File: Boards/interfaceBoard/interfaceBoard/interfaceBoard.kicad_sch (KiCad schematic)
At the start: 0 parts

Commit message: interface board work
started interface board with child sheets. Working on MOSI circuit
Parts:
- added D1, D2: LED, symbol Device:LED
- added J1: Interface With Arduino, symbol Connector_Generic:Conn_02x04_Odd_Even
- added R1, R2: R, symbol Device:R
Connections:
- new net: D1.2 (A), R1.2
- new net: D2.2 (A), R2.2
- new net CLK: J1.2 (Pin_2)
- new net GND: D2.1 (K), J1.1 (Pin_1)
- new net LATCH: J1.5 (Pin_5)
- new net LOAD: J1.6 (Pin_6)
- new net MISO: J1.4 (Pin_4)
- new net MOSI: J1.3 (Pin_3)
- new net STATUS: D1.1 (K), J1.7 (Pin_7), R2.1
- new net VCC: J1.8 (Pin_8), R1.1
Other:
- added sheet output (output.kicad_sch)

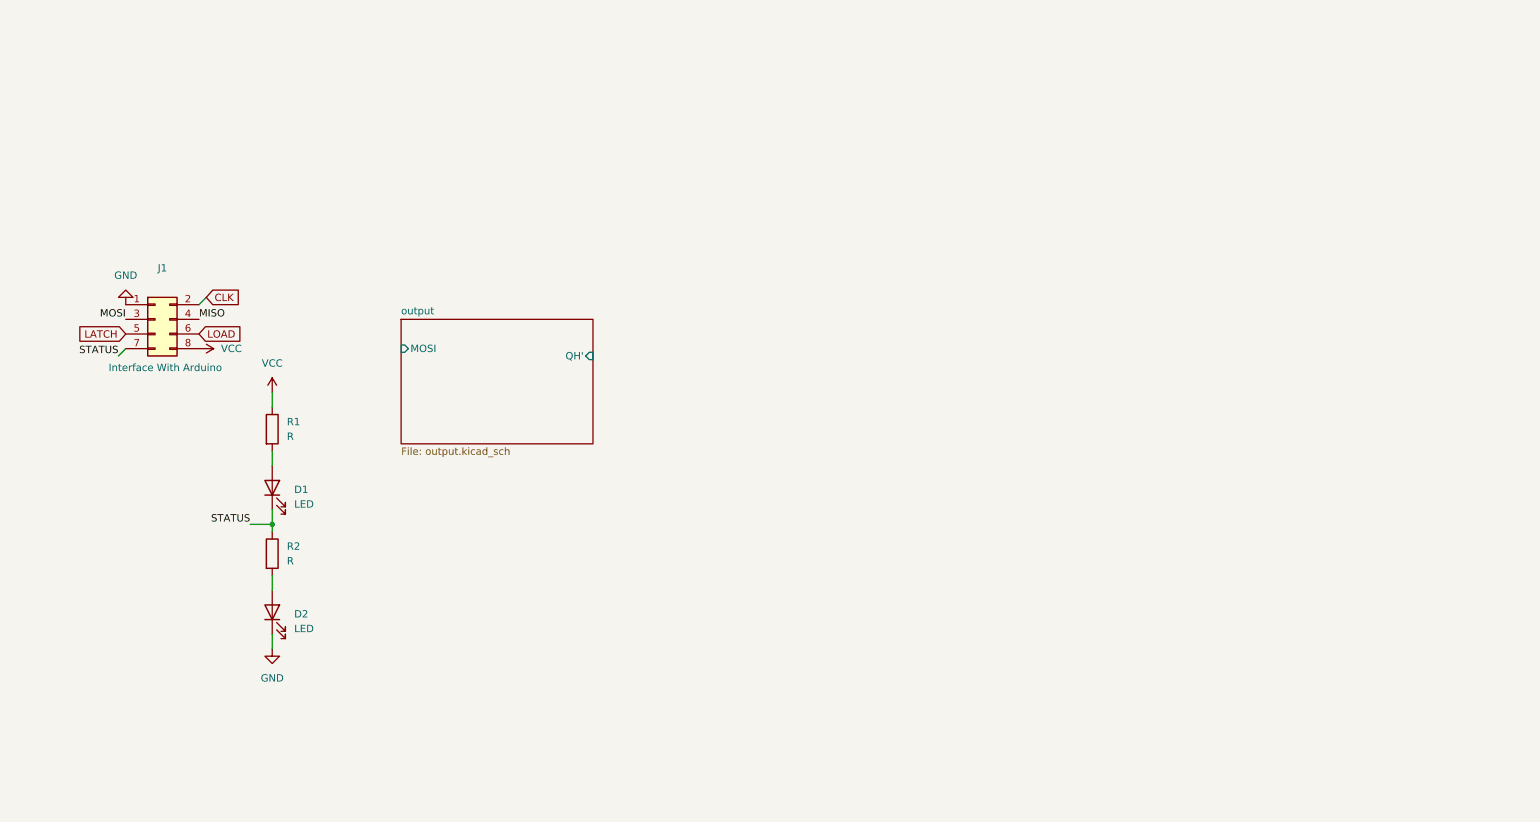
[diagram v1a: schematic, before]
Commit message: interface board work
finished the MOSI child sheet
finished the MISO child sheet
started work on pcb layout (only 1 MOSI and MISO)
started work on pcb layout
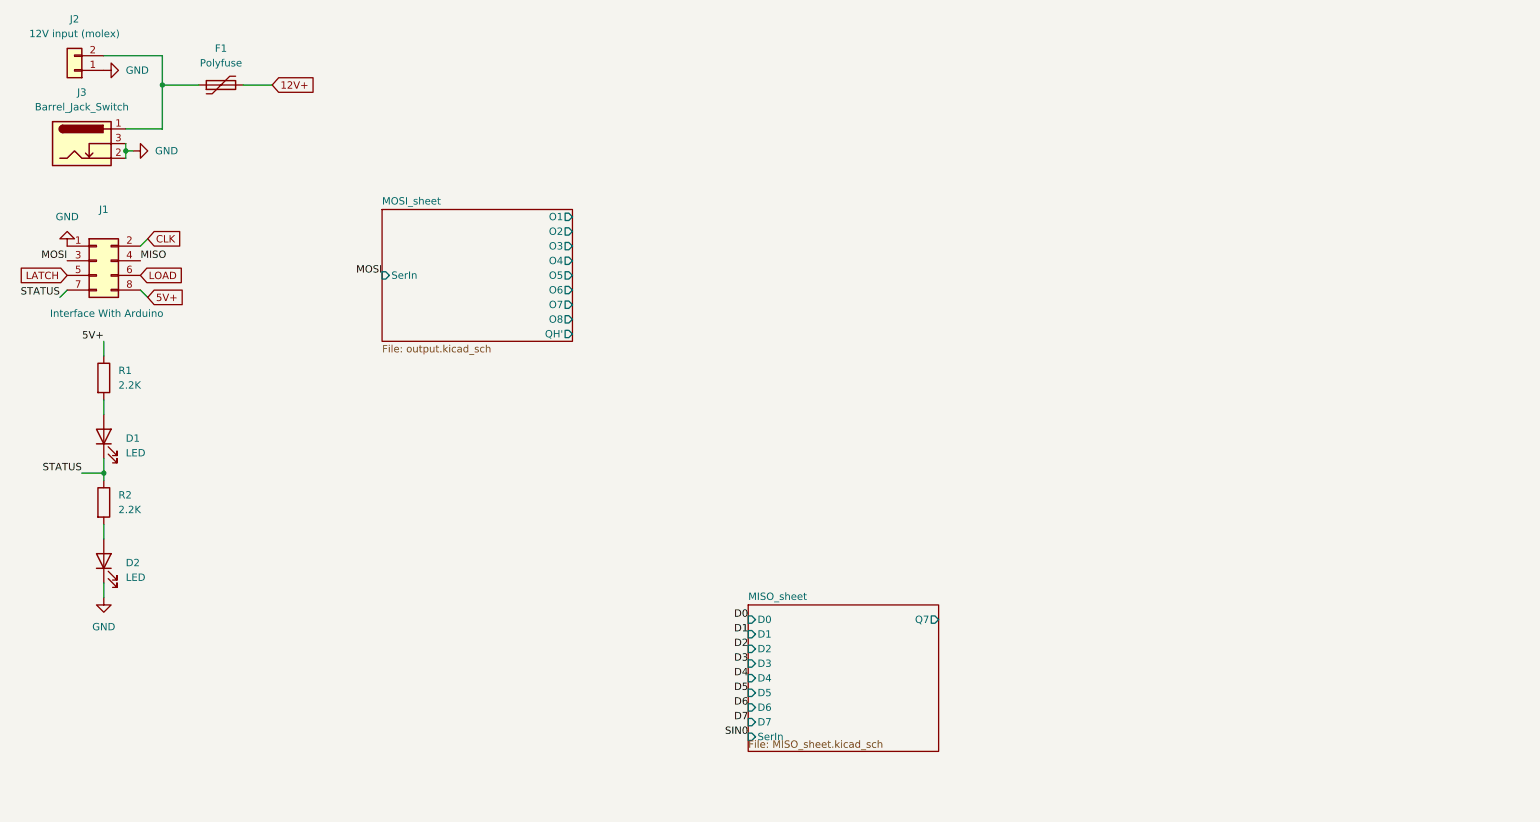
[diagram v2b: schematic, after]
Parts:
- added F1: Polyfuse, Fuse:Fuse_Bourns_MF-RHT100, symbol Device:Polyfuse
- added J2: 12V input (molex), Connector_Molex:Molex_Mini-Fit_Jr_5566-02A_2x01_P4.20mm_Vertical, symbol Connector_Generic:Conn_01x02
- added J3: Barrel_Jack_Switch, Connector_BarrelJack:BarrelJack_Horizontal, symbol Connector:Barrel_Jack_Switch
- D1, D2: footprint (none) -> LED_THT:LED_D3.0mm
- J1: footprint (none) -> Connector_PinHeader_2.54mm:PinHeader_2x04_P2.54mm_Vertical
- R1, R2: value R -> 2.2K; footprint (none) -> Resistor_THT:R_Axial_DIN0207_L6.3mm_D2.5mm_P10.16mm_Horizontal
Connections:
- net GND: now also J2.1 (Pin_1), J3.2, J3.3
- net VCC renamed 5V+
- new net: F1.1, J2.2 (Pin_2), J3.1
- new net 12V+: F1.2
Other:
- sheet output renamed MOSI_sheet
- added sheet MISO_sheet (MISO_sheet.kicad_sch)
- sheet MOSI_sheet ports: added O1, O2, O3, O4, O5, O6, O7, O8, SerIn; removed MOSI
- moved on the sheet: D1, D2, J1, R1, R2

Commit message: interface board added stuff
added more miso and mosi channels

did some placement
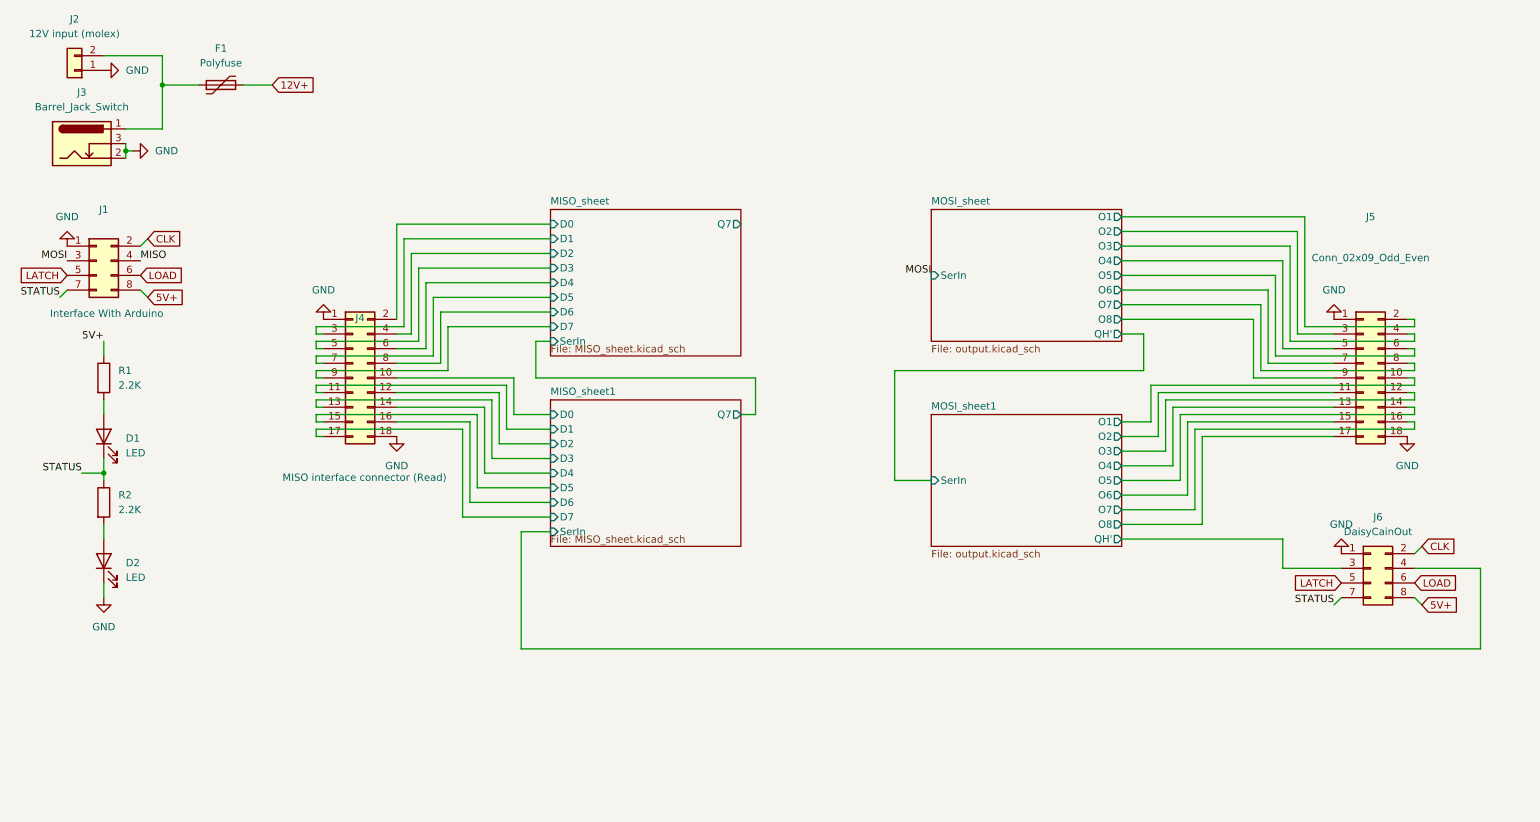
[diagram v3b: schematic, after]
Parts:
- added J4: MISO interface connector (Read), Connector_PinHeader_2.54mm:PinHeader_2x09_P2.54mm_Vertical, symbol Connector_Generic:Conn_02x09_Odd_Even
- added J5: Conn_02x09_Odd_Even, Connector_PinHeader_2.54mm:PinHeader_2x09_P2.54mm_Vertical, symbol Connector_Generic:Conn_02x09_Odd_Even
- added J6: DaisyCainOut, symbol Connector_Generic:Conn_02x04_Odd_Even
- J2: footprint Connector_Molex:Molex_Mini-Fit_Jr_5566-02A_2x01_P4.20mm_Vertical -> molexCustom:CONN_SD-172648-0000_02_MOL
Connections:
- net 5V+: now also J6.8 (Pin_8)
- net CLK: now also J6.2 (Pin_2)
- net GND: now also J4.1 (Pin_1), J4.18 (Pin_18), J5.1 (Pin_1), J5.18 (Pin_18), J6.1 (Pin_1)
- net LATCH: now also J6.5 (Pin_5)
- net LOAD: now also J6.6 (Pin_6)
- net MOSI_sheet/O1: now also J5.2 (Pin_2)
- net MOSI_sheet/O2: now also J5.3 (Pin_3)
- net MOSI_sheet/O3: now also J5.4 (Pin_4)
- net MOSI_sheet/O4: now also J5.5 (Pin_5)
- net MOSI_sheet/O5: now also J5.6 (Pin_6)
- net MOSI_sheet/O6: now also J5.7 (Pin_7)
- net MOSI_sheet/O7: now also J5.8 (Pin_8)
- net MOSI_sheet/O8: now also J5.9 (Pin_9)
- net STATUS: now also J6.7 (Pin_7)
- new net MISO_sheet/D0: J4.2 (Pin_2)
- new net MISO_sheet/D1: J4.3 (Pin_3)
- new net MISO_sheet/D2: J4.4 (Pin_4)
- new net MISO_sheet/D3: J4.5 (Pin_5)
- new net MISO_sheet/D4: J4.6 (Pin_6)
- new net MISO_sheet/D5: J4.7 (Pin_7)
- new net MISO_sheet/D6: J4.8 (Pin_8)
- new net MISO_sheet/D7: J4.9 (Pin_9)
- new net MISO_sheet1/D0: J4.10 (Pin_10)
- new net MISO_sheet1/D1: J4.11 (Pin_11)
- new net MISO_sheet1/D2: J4.12 (Pin_12)
- new net MISO_sheet1/D3: J4.13 (Pin_13)
- new net MISO_sheet1/D4: J4.14 (Pin_14)
- new net MISO_sheet1/D5: J4.15 (Pin_15)
- new net MISO_sheet1/D6: J4.16 (Pin_16)
- new net MISO_sheet1/D7: J4.17 (Pin_17)
- new net MISO_sheet1/SerIn: J6.4 (Pin_4)
- new net MOSI_sheet1/O1: J5.10 (Pin_10)
- new net MOSI_sheet1/O2: J5.11 (Pin_11)
- new net MOSI_sheet1/O3: J5.12 (Pin_12)
- new net MOSI_sheet1/O4: J5.13 (Pin_13)
- new net MOSI_sheet1/O5: J5.14 (Pin_14)
- new net MOSI_sheet1/O6: J5.15 (Pin_15)
- new net MOSI_sheet1/O7: J5.16 (Pin_16)
- new net MOSI_sheet1/O8: J5.17 (Pin_17)
- new net MOSI_sheet1/QH': J6.3 (Pin_3)
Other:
- added sheet MISO_sheet1 (MISO_sheet.kicad_sch)
- added sheet MOSI_sheet1 (output.kicad_sch)

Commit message: Big progress
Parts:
- removed J4: MISO interface connector (Read), Connector_PinHeader_2.54mm:PinHeader_2x09_P2.54mm_Vertical, symbol Connector_Generic:Conn_02x09_Odd_Even
- removed J5: Conn_02x09_Odd_Even, Connector_PinHeader_2.54mm:PinHeader_2x09_P2.54mm_Vertical, symbol Connector_Generic:Conn_02x09_Odd_Even
- added D3: LED, LED_THT:LED_D3.0mm, symbol Device:LED
- added J4, J5: Conn_02x17_Odd_Even, Connector_PinHeader_2.54mm:PinHeader_2x17_P2.54mm_Vertical, symbol Connector_Generic:Conn_02x17_Odd_Even
- added R3: R, Resistor_THT:R_Axial_DIN0207_L6.3mm_D2.5mm_P10.16mm_Horizontal, symbol Device:R
- added SW1: SW_SPDT, myLibrary:SW_SPDT_SS-12D10L5, symbol Switch:SW_SPDT
- J6: footprint (none) -> Connector_PinHeader_2.54mm:PinHeader_2x04_P2.54mm_Vertical
- renumbered J2 to J1, J3 to J2, J1 to J3
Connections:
- net 12V+: now also R3.1
- net GND: now also D3.1 (K), J4.1 (Pin_1), J4.34 (Pin_34), J5.1 (Pin_1), J5.34 (Pin_34)
- net MISO_sheet/D0: now also J5.2 (Pin_2)
- net MISO_sheet/D1: now also J5.3 (Pin_3)
- net MISO_sheet/D2: now also J5.4 (Pin_4)
- net MISO_sheet/D3: now also J5.5 (Pin_5)
- net MISO_sheet/D4: now also J5.6 (Pin_6)
- net MISO_sheet/D5: now also J5.7 (Pin_7)
- net MISO_sheet/D6: now also J5.8 (Pin_8)
- net MISO_sheet/D7: now also J5.9 (Pin_9)
- net MISO_sheet1/D0: now also J5.10 (Pin_10)
- net MISO_sheet1/D1: now also J5.11 (Pin_11)
- net MISO_sheet1/D2: now also J5.12 (Pin_12)
- net MISO_sheet1/D3: now also J5.13 (Pin_13)
- net MISO_sheet1/D4: now also J5.14 (Pin_14)
- net MISO_sheet1/D5: now also J5.15 (Pin_15)
- net MISO_sheet1/D6: now also J5.16 (Pin_16)
- net MISO_sheet1/D7: now also J5.17 (Pin_17)
- net MISO_sheet1/SerIn: no longer J6.4 (Pin_4)
- net MOSI_sheet/O1: now also J4.2 (Pin_2)
- net MOSI_sheet/O2: now also J4.3 (Pin_3)
- net MOSI_sheet/O3: now also J4.4 (Pin_4)
- net MOSI_sheet/O4: now also J4.5 (Pin_5)
- net MOSI_sheet/O5: now also J4.6 (Pin_6)
- net MOSI_sheet/O6: now also J4.7 (Pin_7)
- net MOSI_sheet/O7: now also J4.8 (Pin_8)
- net MOSI_sheet/O8: now also J4.9 (Pin_9)
- net MOSI_sheet1/O1: now also J4.10 (Pin_10)
- net MOSI_sheet1/O2: now also J4.11 (Pin_11)
- net MOSI_sheet1/O3: now also J4.12 (Pin_12)
- net MOSI_sheet1/O4: now also J4.13 (Pin_13)
- net MOSI_sheet1/O5: now also J4.14 (Pin_14)
- net MOSI_sheet1/O6: now also J4.15 (Pin_15)
- net MOSI_sheet1/O7: now also J4.16 (Pin_16)
- net MOSI_sheet1/O8: now also J4.17 (Pin_17)
- net MOSI_sheet1/QH': no longer J6.3 (Pin_3)
- new net: J1.2 (Pin_2), SW1.3 (C)
- new net: D3.2 (A), R3.2
- new net: J2.1, SW1.1 (A)
- new net: F1.1, SW1.2 (B)
- new net MISO_sheet2/D0: J5.18 (Pin_18)
- new net MISO_sheet2/D1: J5.19 (Pin_19)
- new net MISO_sheet2/D2: J5.20 (Pin_20)
- new net MISO_sheet2/D3: J5.21 (Pin_21)
- new net MISO_sheet2/D4: J5.22 (Pin_22)
- new net MISO_sheet2/D5: J5.23 (Pin_23)
- new net MISO_sheet2/D6: J5.24 (Pin_24)
- new net MISO_sheet2/D7: J5.25 (Pin_25)
- new net MISO_sheet3/D0: J5.26 (Pin_26)
- new net MISO_sheet3/D1: J5.27 (Pin_27)
- new net MISO_sheet3/D2: J5.28 (Pin_28)
- new net MISO_sheet3/D3: J5.29 (Pin_29)
- new net MISO_sheet3/D4: J5.30 (Pin_30)
- new net MISO_sheet3/D5: J5.31 (Pin_31)
- new net MISO_sheet3/D6: J5.32 (Pin_32)
- new net MISO_sheet3/D7: J5.33 (Pin_33)
- new net MISO_sheet3/SerIn: J6.4 (Pin_4)
- new net MOSI_sheet2/O1: J4.18 (Pin_18)
- new net MOSI_sheet2/O2: J4.19 (Pin_19)
- new net MOSI_sheet2/O3: J4.20 (Pin_20)
- new net MOSI_sheet2/O4: J4.21 (Pin_21)
- new net MOSI_sheet2/O5: J4.22 (Pin_22)
- new net MOSI_sheet2/O6: J4.23 (Pin_23)
- new net MOSI_sheet2/O7: J4.24 (Pin_24)
- new net MOSI_sheet2/O8: J4.25 (Pin_25)
- new net MOSI_sheet3/O1: J4.26 (Pin_26)
- new net MOSI_sheet3/O2: J4.27 (Pin_27)
- new net MOSI_sheet3/O3: J4.28 (Pin_28)
- new net MOSI_sheet3/O4: J4.29 (Pin_29)
- new net MOSI_sheet3/O5: J4.30 (Pin_30)
- new net MOSI_sheet3/O6: J4.31 (Pin_31)
- new net MOSI_sheet3/O7: J4.32 (Pin_32)
- new net MOSI_sheet3/O8: J4.33 (Pin_33)
- new net MOSI_sheet3/QH': J6.3 (Pin_3)
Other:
- added sheet MISO_sheet2 (MISO_sheet.kicad_sch)
- added sheet MISO_sheet3 (MISO_sheet.kicad_sch)
- added sheet MOSI_sheet2 (output.kicad_sch)
- added sheet MOSI_sheet3 (output.kicad_sch)
- moved on the sheet: F1, J6

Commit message: MOSI done?
MOSI wired.
MISO wired to interface
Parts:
- renumbered J5 to J4, J6 to J5, J4 to J6
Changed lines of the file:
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@@
 		(dnp no)
 		(fields_autoplaced yes)
-		(property "Reference" "#PWR038"
+		(property "Reference" "#PWR05"
 			(at 67.31 54.61 0)
 			(hide yes)
@@
 			(project "interfaceBoard"
 				(path "/235e1922-7e9c-45bb-adad-cde682cd8f35"
-					(reference "#PWR038")
+					(reference "#PWR05")
 					(unit 1)
 				)
@@
 		(dnp no)
 		(fields_autoplaced yes)
-		(property "Reference" "#PWR08"
+		(property "Reference" "#PWR07"
 			(at 90.17 110.49 0)
 			(hide yes)
@@
 			(project "interfaceBoard"
 				(path "/235e1922-7e9c-45bb-adad-cde682cd8f35"
-					(reference "#PWR08")
+					(reference "#PWR07")
 					(unit 1)
 				)
@@
 		(dnp no)
 		(fields_autoplaced yes)
-		(property "Reference" "J4"
+		(property "Reference" "J6"
 			(at 269.24 57.15 0)
 			(show_name no)
@@
 			(project "interfaceBoard"
 				(path "/235e1922-7e9c-45bb-adad-cde682cd8f35"
-					(reference "J4")
+					(reference "J6")
 					(unit 1)
 				)
@@
 		(dnp no)
 		(fields_autoplaced yes)
-		(property "Reference" "J6"
+		(property "Reference" "J5"
 			(at 257.81 135.89 0)
 			(show_name no)
@@
 			(project "interfaceBoard"
 				(path "/235e1922-7e9c-45bb-adad-cde682cd8f35"
-					(reference "J6")
+					(reference "J5")
 					(unit 1)
 				)
@@
 		(dnp no)
 		(fields_autoplaced yes)
-		(property "Reference" "#PWR05"
+		(property "Reference" "#PWR09"
 			(at 262.89 57.15 0)
 			(hide yes)
@@
 			(project "interfaceBoard"
 				(path "/235e1922-7e9c-45bb-adad-cde682cd8f35"
-					(reference "#PWR05")
+					(reference "#PWR09")
 					(unit 1)
 				)
@@
 		(dnp no)
 		(fields_autoplaced yes)
-		(property "Reference" "#PWR07"
+		(property "Reference" "#PWR06"
 			(at 77.47 57.15 0)
 			(hide yes)
@@
 			(project "interfaceBoard"
 				(path "/235e1922-7e9c-45bb-adad-cde682cd8f35"
-					(reference "#PWR07")
+					(reference "#PWR06")
 					(unit 1)
 				)
@@
 		(dnp no)
 		(fields_autoplaced yes)
-		(property "Reference" "#PWR09"
+		(property "Reference" "#PWR08"
 			(at 251.46 135.89 0)
 			(hide yes)
@@
 			(project "interfaceBoard"
 				(path "/235e1922-7e9c-45bb-adad-cde682cd8f35"
-					(reference "#PWR09")
+					(reference "#PWR08")
 					(unit 1)
 				)
@@
 		(dnp no)
 		(fields_autoplaced yes)
-		(property "Reference" "J5"
+		(property "Reference" "J4"
 			(at 83.82 57.15 0)
 			(show_name no)
@@
 			(project "interfaceBoard"
 				(path "/235e1922-7e9c-45bb-adad-cde682cd8f35"
-					(reference "J5")
+					(reference "J4")
 					(unit 1)
 				)
@@
 		(dnp no)
 		(fields_autoplaced yes)
-		(property "Reference" "#PWR06"
+		(property "Reference" "#PWR010"
 			(at 275.59 110.49 0)
 			(hide yes)
@@
 			(project "interfaceBoard"
 				(path "/235e1922-7e9c-45bb-adad-cde682cd8f35"
-					(reference "#PWR06")
+					(reference "#PWR010")
 					(unit 1)
 				)
@@
 			(project "interfaceBoard"
 				(path "/235e1922-7e9c-45bb-adad-cde682cd8f35"
-					(page "4")
+					(page "7")
 				)
 			)
@@
 			(project "interfaceBoard"
 				(path "/235e1922-7e9c-45bb-adad-cde682cd8f35"
-					(page "12")
+					(page "4")
 				)
 			)
@@
 			(project "interfaceBoard"
 				(path "/235e1922-7e9c-45bb-adad-cde682cd8f35"
-					(page "13")
+					(page "5")
 				)
 			)
@@
 			(project "interfaceBoard"
 				(path "/235e1922-7e9c-45bb-adad-cde682cd8f35"
-					(page "5")
+					(page "9")
 				)
 			)
@@
 			(project "interfaceBoard"
 				(path "/235e1922-7e9c-45bb-adad-cde682cd8f35"
-					(page "7")
+					(page "8")
 				)
 			)
